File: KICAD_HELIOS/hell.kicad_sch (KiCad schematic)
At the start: 27 parts, among them J1 Conn_01x05, J3 NC3FAAH, J4 NC3MAAH, J5 ecran, SW1 SW_Push, SW2 SW_Push, U1 STM32F103C6Tx, U2 AMS1117-3.3, U3 MAX485E, U4 R-78B2.5-2.0

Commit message: Fix: correction erreurs schéma, maj empreintes et ajout notes
- Résolution de toutes les erreurs ERC du schéma.
- Mise à jour des empreintes (Importation d'empreintes non présentes dans KiCad, composants passifs...).
- Ajout de Warning_KiCad_fichier_temporaire.md : liste des questions et problèmes à régler.
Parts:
- C1, C10, C12, C2, C3, C4, C5, C6, C7, C8, C9: footprint (none) -> Capacitor_SMD:C_0805_2012Metric
- D1, D2: footprint (none) -> LED_SMD:LED_0805_2012Metric
- J1, J5: footprint (none) -> Connector_PinHeader_2.54mm:PinHeader_1x05_P2.54mm_Vertical
- R1, R2: footprint (none) -> Resistor_SMD:R_0805_2012Metric
- R3, R4: footprint (none) -> Resistor_SMD:R_1210_3225Metric
- SW1, SW2: footprint (none) -> Button_Switch_THT:SW_PUSH_6mm
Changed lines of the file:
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@@
 			)
 		)
-		(property "Footprint" ""
+		(property "Footprint" "Capacitor_SMD:C_0805_2012Metric"
 			(at 34.29 100.33 0)
 			(effects
@@
 			)
 		)
-		(property "Footprint" ""
+		(property "Footprint" "Capacitor_SMD:C_0805_2012Metric"
 			(at 220.98 36.83 0)
 			(effects
@@
 			)
 		)
-		(property "Footprint" ""
+		(property "Footprint" "Capacitor_SMD:C_0805_2012Metric"
 			(at 201.93 67.31 0)
 			(effects
@@
 			)
 		)
-		(property "Footprint" ""
+		(property "Footprint" "Capacitor_SMD:C_0805_2012Metric"
 			(at 80.01 88.9 0)
 			(effects
@@
 			)
 		)
-		(property "Footprint" ""
+		(property "Footprint" "Resistor_SMD:R_1210_3225Metric"
 			(at 187.96 130.81 0)
 			(effects
@@
 			)
 		)
-		(property "Footprint" ""
+		(property "Footprint" "Resistor_SMD:R_0805_2012Metric"
 			(at 29.21 100.33 0)
 			(effects
@@
 			)
 		)
-		(property "Footprint" ""
+		(property "Footprint" "Resistor_SMD:R_1210_3225Metric"
 			(at 187.96 120.65 0)
 			(effects
@@
 			)
 		)
-		(property "Footprint" ""
+		(property "Footprint" "Capacitor_SMD:C_0805_2012Metric"
 			(at 101.6 88.9 0)
 			(effects
@@
 			)
 		)
-		(property "Footprint" ""
+		(property "Footprint" "Capacitor_SMD:C_0805_2012Metric"
 			(at 86.36 88.9 0)
 			(effects
@@
 			)
 		)
-		(property "Footprint" ""
+		(property "Footprint" "Button_Switch_THT:SW_PUSH_6mm"
 			(at 149.86 127 0)
 			(effects
@@
 			)
 		)
-		(property "Footprint" ""
+		(property "Footprint" "LED_SMD:LED_0805_2012Metric"
 			(at 194.31 130.81 0)
 			(effects
@@
 			)
 		)
-		(property "Footprint" ""
+		(property "Footprint" "Connector_PinHeader_2.54mm:PinHeader_1x05_P2.54mm_Vertical"
 			(at 106.68 116.84 0)
 			(effects
@@
 			)
 		)
-		(property "Footprint" ""
+		(property "Footprint" "LED_SMD:LED_0805_2012Metric"
 			(at 194.31 120.65 0)
 			(effects
@@
 			)
 		)
-		(property "Footprint" ""
+		(property "Footprint" "Capacitor_SMD:C_0805_2012Metric"
 			(at 219.71 41.91 0)
 			(effects
@@
 			)
 		)
-		(property "Footprint" ""
+		(property "Footprint" "Resistor_SMD:R_0805_2012Metric"
 			(at 34.29 105.41 0)
 			(effects
@@
 			)
 		)
-		(property "Footprint" ""
+		(property "Footprint" "Connector_PinHeader_2.54mm:PinHeader_1x05_P2.54mm_Vertical"
 			(at 180.34 99.06 0)
 			(effects
@@
 			)
 		)
-		(property "Footprint" ""
+		(property "Footprint" "Capacitor_SMD:C_0805_2012Metric"
 			(at 166.37 95.25 0)
 			(effects
@@
 			)
 		)
-		(property "Footprint" ""
+		(property "Footprint" "Capacitor_SMD:C_0805_2012Metric"
 			(at 232.41 67.31 0)
 			(effects
@@
 			)
 		)
-		(property "Footprint" ""
+		(property "Footprint" "Capacitor_SMD:C_0805_2012Metric"
 			(at 92.71 88.9 0)
 			(effects
@@
 			)
 		)
-		(property "Footprint" ""
+		(property "Footprint" "Button_Switch_THT:SW_PUSH_6mm"
 			(at 151.13 118.11 0)
 			(effects
@@
 			)
 		)
-		(property "Footprint" ""
+		(property "Footprint" "Capacitor_SMD:C_0805_2012Metric"
 			(at 110.49 88.9 0)
 			(effects

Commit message: changement à faire schématic
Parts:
- removed U4: R-78B2.5-2.0, Converter_DCDC:Converter_DCDC_RECOM_R-78B-2.0_THT, symbol Converter_DCDC:R-78B2.5-2.0
- added J2: Conn_ST_STDC14, symbol Connector:Conn_ST_STDC14
- added U11: R-78B2.5-2.0, Converter_DCDC:Converter_DCDC_RECOM_R-78B-2.0_THT, symbol Converter_DCDC:R-78B2.5-2.0
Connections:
- net +24V: now also U11.1 (IN)
- net +5V: now also C7.1, U11.3 (OUT); no longer C7.2
- net GND: now also C7.2, U11.2 (GND); no longer C7.1
- new net: J2.5 (GND), J2.7 (GND)
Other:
- note added: "<-remplacer par ->"
- note added: "augmenter R"
- note added: "changer pour que ça soit mieux"
- note added: "changer valeur"
- note added: "condensateur"
- note added: "problème avec I2C"
- moved on the sheet: C6, C7, C8, C9, J1, U2

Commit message: correction (reste à calculer L)
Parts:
- removed J1: Conn_01x05, Connector_PinHeader_2.54mm:PinHeader_1x05_P2.54mm_Vertical, symbol Connector_Generic:Conn_01x05
- removed SW2: SW_Push, Button_Switch_THT:SW_PUSH_6mm, symbol Switch:SW_Push
- added C24: 100n, Capacitor_SMD:C_0805_2012Metric, symbol Device:C_Small
- added C25, C26: 10n, Capacitor_SMD:C_0805_2012Metric, symbol Device:C_Small
- added R13, R14, R15, R6: 10k, Resistor_SMD:R_1210_3225Metric, symbol Device:R_Small
- added R5: 1k, Resistor_SMD:R_1210_3225Metric, symbol Device:R_Small
- added SW3, SW4: SW_Push, Button_Switch_THT:SW_PUSH_6mm, symbol Switch:SW_Push
- C10: value 100u -> 1u
- C6, C7: value 100n -> 10u
- C9: value 10u -> 22u
- D1, D2: MPN (none) -> 150060RS55040
- R1: value 10k -> 1k; footprint Resistor_SMD:R_0805_2012Metric -> Resistor_SMD:R_1210_3225Metric
- R3, R4: value 330 -> 1k6
- U11: value R-78B2.5-2.0 -> R-78B5.0-2.0; MPN (none) -> R-78B5.0-2.0
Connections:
- net NRST is gone; now on net +3.3V: C12.2, U1.7 (NRST)
- net +3.3V: now also J2.12 (~{RST}), J2.3 (VCC), R1.2, R15.1, R5.2, R6.1, SW3.2; no longer R1.1, SW1.2
- net +5V: now also C24.1
- net BOUTTON_1: now also C25.1, R13.1; no longer SW1.1
- net BOUTTON_2: now also C26.1, R14.1
- net Ecr_SCL: now also R1.1
- net Ecr_SDA: now also R5.1
- net GND: now also C12.1, J2.11 (GNDDetect), J2.5 (GND), J2.7 (GND), SW1.2, C24.2, C25.2, C26.2, SW3.1, SW4.2
- net SWCLK: now also J2.6 (JCLK/SWCLK)
- net SWDIO: now also J2.4 (JTMS/SWDIO)
- new net: R13.2, R6.2, SW1.1
- new net: R14.2, R15.2, SW4.1
- no-connect marks 23 -> 28
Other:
- note added: "1.7V @ 1mA"
- note removed: "<-remplacer par ->"
- note removed: "augmenter R"
- note removed: "changer pour que ça soit mieux"
- note removed: "changer valeur"
- note removed: "condensateur"
- note removed: "problème avec I2C"
- moved on the sheet: C12, D1, D2, J2, R3, R4, SW1

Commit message: schématic finie
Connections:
- net +3.3V: no longer C12.2, J2.12 (~{RST}), SW3.2, U1.7 (NRST)
- new net NRST: C12.2, J2.12 (~{RST}), SW3.2, U1.7 (NRST)
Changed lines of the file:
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@@
 	)
 	(junction
-		(at 26.67 91.44)
-		(diameter 0)
-		(color 0 0 0 0)
-	)
-	(junction
 		(at 213.36 29.21)
 		(diameter 0)
@@
 	(wire
 		(pts
-			(xy 26.67 90.17) (xy 26.67 91.44)
-		)
-		(stroke
-			(width 0)
-			(type default)
-		)
-	)
-	(wire
-		(pts
 			(xy 187.96 38.1) (xy 199.39 38.1)
 		)
@@
 					(unit 1)
 				)
-			)
-		)
-	)
-	(symbol
-		(lib_id "power:+3.3V")
-		(at 26.67 90.17 0)
-		(unit 1)
-		(exclude_from_sim no)
-		(in_bom yes)
-		(on_board yes)
-		(dnp no)
-		(fields_autoplaced yes)
-		(property "Reference" "#PWR07"
-			(at 26.67 93.98 0)
-			(effects
-				(font
-					(size 1.27 1.27)
-				)
-				(hide yes)
-			)
-		)
-		(property "Value" "+3.3V"
-			(at 26.67 85.09 0)
-			(effects
-				(font
-					(size 1.27 1.27)
-				)
-			)
-		)
-		(property "Footprint" ""
-			(at 26.67 90.17 0)
-			(effects
-				(font
-					(size 1.27 1.27)
-				)
-				(hide yes)
-			)
-		)
-		(property "Datasheet" ""
-			(at 26.67 90.17 0)
-			(effects
-				(font
-					(size 1.27 1.27)
-				)
-				(hide yes)
-			)
-		)
-		(property "Description" "Power symbol creates a global label with name \"+3.3V\""
-			(at 26.67 90.17 0)
-			(effects
-				(font
-					(size 1.27 1.27)
-				)
-				(hide yes)
-			)
-		)
-		(pin "1"
-		)
-		(instances
-			(project "hell"
-				(path "/c000bab8-8bf2-446c-9c19-e9a7fa645af1"
-					(reference "#PWR07")
-					(unit 1)
-				)

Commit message: schematic + empreinte
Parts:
- J2: footprint (none) -> Connector_PinHeader_1.27mm:PinHeader_2x07_P1.27mm_Vertical_SMD
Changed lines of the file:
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@@
 			)
 		)
-		(property "Footprint" ""
+		(property "Footprint" "Connector_PinHeader_1.27mm:PinHeader_2x07_P1.27mm_Vertical_SMD"
 			(at 102.87 161.29 0)
 			(effects

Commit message: update pcb
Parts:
- added H101, H102, H103, H104, H105, H106: MountingHole_Pad, MountingHole:MountingHole_3.2mm_M3_DIN965_Pad, symbol Mechanical:MountingHole_Pad
- added J105: Conn_01x02, Connector_AMASS:AMASS_XT30U-M_1x02_P5.0mm_Vertical, symbol Connector_Generic:Conn_01x02
- renumbered C6 to C101, C7 to C102, C8 to C103, C9 to C104, C24 to C105, C5 to C106, C4 to C107, C1 to C108, C2 to C109, C3 to C110, C10 to C111, C12 to C112, C26 to C113, C25 to C114, D1 to D101, D2 to D102, J3 to J101, J4 to J102, J5 to J103, J2 to J104, R15 to R101, R1 to R102, R5 to R103, R6 to R104, R14 to R105, R13 to R106, R2 to R107, R3 to R108, R4 to R109, SW3 to SW101, SW4 to SW102, SW1 to SW103, U11 to U101, U2 to U102, U3 to U103, U1 to U104
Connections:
- net +24V: now also J105.2 (Pin_2)
- net GND: now also H101.1, H102.1, H103.1, H104.1, H105.1, H106.1, J105.1 (Pin_1)

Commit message: Kicad PCB et changement de quelques empreintes
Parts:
- C101: footprint Capacitor_SMD:C_0805_2012Metric -> Capacitor_SMD:C_1206_3216Metric
- C102, C103: footprint Capacitor_SMD:C_0805_2012Metric -> Capacitor_SMD:C_0603_1608Metric
- C105, C106, C107, C108, C109, C110, C111, C112, C113, C114: footprint Capacitor_SMD:C_0805_2012Metric -> Capacitor_SMD:C_0402_1005Metric
- R104, R105, R106: footprint Resistor_SMD:R_1210_3225Metric -> Resistor_SMD:R_0805_2012Metric
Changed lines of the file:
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@@
 			)
 		)
-		(property "Footprint" "Capacitor_SMD:C_0805_2012Metric"
+		(property "Footprint" "Capacitor_SMD:C_0402_1005Metric"
 			(at 30.48 100.33 0)
 			(effects
@@
 			)
 		)
-		(property "Footprint" "Capacitor_SMD:C_0805_2012Metric"
+		(property "Footprint" "Capacitor_SMD:C_1206_3216Metric"
 			(at 187.96 33.02 0)
 			(effects
@@
 			)
 		)
-		(property "Footprint" "Capacitor_SMD:C_0805_2012Metric"
+		(property "Footprint" "Capacitor_SMD:C_0603_1608Metric"
 			(at 228.6 52.07 0)
 			(effects
@@
 			)
 		)
-		(property "Footprint" "Capacitor_SMD:C_0805_2012Metric"
+		(property "Footprint" "Capacitor_SMD:C_0402_1005Metric"
 			(at 80.01 88.9 0)
 			(effects
@@
 			)
 		)
-		(property "Footprint" "Capacitor_SMD:C_0805_2012Metric"
+		(property "Footprint" "Capacitor_SMD:C_0402_1005Metric"
 			(at 210.82 107.95 0)
 			(effects
@@
 			)
 		)
-		(property "Footprint" "Resistor_SMD:R_1210_3225Metric"
+		(property "Footprint" "Resistor_SMD:R_0805_2012Metric"
 			(at 220.98 97.79 0)
 			(effects
@@
 			)
 		)
-		(property "Footprint" "Resistor_SMD:R_1210_3225Metric"
+		(property "Footprint" "Resistor_SMD:R_0805_2012Metric"
 			(at 255.27 100.33 0)
 			(effects
@@
 			)
 		)
-		(property "Footprint" "Capacitor_SMD:C_0805_2012Metric"
+		(property "Footprint" "Capacitor_SMD:C_0402_1005Metric"
 			(at 101.6 88.9 0)
 			(effects
@@
 			)
 		)
-		(property "Footprint" "Capacitor_SMD:C_0805_2012Metric"
+		(property "Footprint" "Capacitor_SMD:C_0402_1005Metric"
 			(at 250.19 106.68 0)
 			(effects
@@
 			)
 		)
-		(property "Footprint" "Capacitor_SMD:C_0805_2012Metric"
+		(property "Footprint" "Capacitor_SMD:C_0402_1005Metric"
 			(at 86.36 88.9 0)
 			(effects
@@
 			)
 		)
-		(property "Footprint" "Capacitor_SMD:C_0805_2012Metric"
+		(property "Footprint" "Capacitor_SMD:C_0603_1608Metric"
 			(at 213.36 33.02 0)
 			(effects
@@
 			)
 		)
-		(property "Footprint" "Capacitor_SMD:C_0805_2012Metric"
+		(property "Footprint" "Capacitor_SMD:C_0402_1005Metric"
 			(at 152.4 67.31 0)
 			(effects
@@
 			)
 		)
-		(property "Footprint" "Capacitor_SMD:C_0805_2012Metric"
+		(property "Footprint" "Capacitor_SMD:C_0402_1005Metric"
 			(at 166.37 95.25 0)
 			(effects
@@
 			)
 		)
-		(property "Footprint" "Capacitor_SMD:C_0805_2012Metric"
+		(property "Footprint" "Capacitor_SMD:C_0402_1005Metric"
 			(at 92.71 88.9 0)
 			(effects
@@
 			)
 		)
-		(property "Footprint" "Resistor_SMD:R_1210_3225Metric"
+		(property "Footprint" "Resistor_SMD:R_0805_2012Metric"
 			(at 215.9 101.6 0)
 			(effects
@@
 			)
 		)
-		(property "Footprint" "Capacitor_SMD:C_0805_2012Metric"
+		(property "Footprint" "Capacitor_SMD:C_0402_1005Metric"
 			(at 110.49 88.9 0)
 			(effects

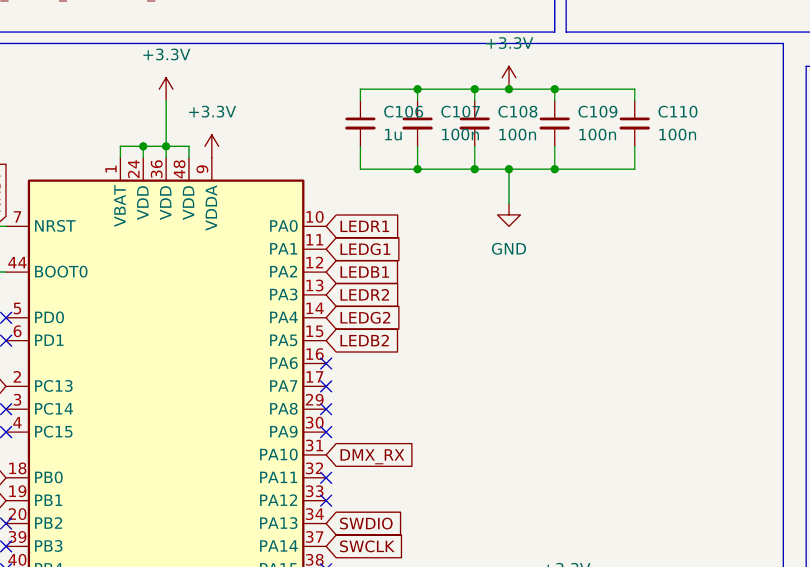
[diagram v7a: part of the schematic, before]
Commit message: Routage presque fini en attente de modification d'empreinte
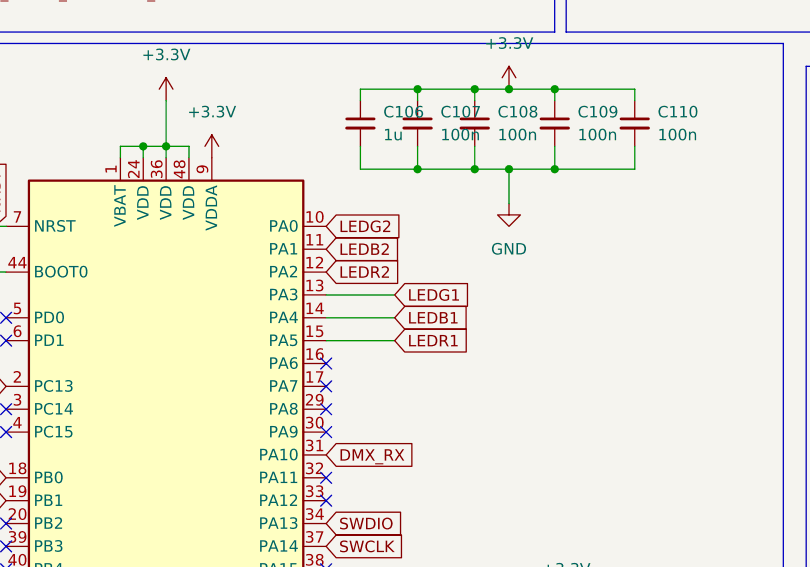
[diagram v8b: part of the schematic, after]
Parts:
- D101, D102: footprint LED_SMD:LED_0805_2012Metric -> LED_SMD:LED_0603_1608Metric
- R101, R102, R103, R108, R109: footprint Resistor_SMD:R_1210_3225Metric -> Resistor_SMD:R_0603_1608Metric
- R104, R105, R106, R107: footprint Resistor_SMD:R_0805_2012Metric -> Resistor_SMD:R_0603_1608Metric
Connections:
- net LEDB1: now also U104.14 (PA4); no longer U104.12 (PA2)
- net LEDB2: now also U104.11 (PA1); no longer U104.15 (PA5)
- net LEDG1: now also U104.13 (PA3); no longer U104.11 (PA1)
- net LEDG2: now also U104.10 (PA0); no longer U104.14 (PA4)
- net LEDR1: now also U104.15 (PA5); no longer U104.10 (PA0)
- net LEDR2: now also U104.12 (PA2); no longer U104.13 (PA3)
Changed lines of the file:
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@@
 	(wire
 		(pts
+			(xy 83.82 110.49) (xy 76.2 110.49)
+		)
+		(stroke
+			(width 0)
+			(type default)
+		)
+	)
+	(wire
+		(pts
 			(xy 220.98 100.33) (xy 220.98 101.6)
 		)
@@
 	(wire
 		(pts
+			(xy 83.82 107.95) (xy 76.2 107.95)
+		)
+		(stroke
+			(width 0)
+			(type default)
+		)
+	)
+	(wire
+		(pts
 			(xy 101.6 85.09) (xy 110.49 85.09)
 		)
@@
 	(wire
 		(pts
+			(xy 83.82 113.03) (xy 76.2 113.03)
+		)
+		(stroke
+			(width 0)
+			(type default)
+		)
+	)
+	(wire
+		(pts
 			(xy 119.38 148.59) (xy 115.57 148.59)
 		)
@@
 		)
 	)
+	(global_label "LEDR2"
+		(shape input)
+		(at 76.2 105.41 0)
+		(fields_autoplaced yes)
+		(effects
+			(font
+				(size 1.27 1.27)
+			)
+			(justify left)
+		)
+		(property "Intersheetrefs" "${INTERSHEET_REFS}"
+			(at 85.1118 105.41 0)
+			(effects
+				(font
+					(size 1.27 1.27)
+				)
+				(justify left)
+				(hide yes)
+			)
+		)
+	)
 	(global_label "LEDG1"
 		(shape input)
@@
 		)
 	)
-	(global_label "LED_1"
+	(global_label "LEDG2"
 		(shape input)
-		(at 40.64 128.27 180)
+		(at 76.2 100.33 0)
 		(fields_autoplaced yes)
 		(effects
@@
 				(size 1.27 1.27)
 			)
-			(justify right)
+			(justify left)
 		)
 		(property "Intersheetrefs" "${INTERSHEET_REFS}"
-			(at 32.0306 128.27 0)
+			(at 85.1118 100.33 0)
 			(effects
 				(font
 					(size 1.27 1.27)
 				)
-				(justify right)
+				(justify left)
 				(hide yes)
 			)
 		)
 	)
-	(global_label "DMX_N"
+	(global_label "LED_1"
 		(shape input)
-		(at 142.24 54.61 0)
+		(at 40.64 128.27 180)
 		(fields_autoplaced yes)
 		(effects
@@
 				(size 1.27 1.27)
 			)
-			(justify left)
+			(justify right)
 		)
 		(property "Intersheetrefs" "${INTERSHEET_REFS}"
-			(at 151.4542 54.61 0)
+			(at 32.0306 128.27 0)
 			(effects
 				(font
 					(size 1.27 1.27)
 				)
-				(justify left)
+				(justify right)
 				(hide yes)
 			)
 		)
 	)
-	(global_label "LEDG2"
+	(global_label "DMX_N"
 		(shape input)
-		(at 76.2 110.49 0)
+		(at 142.24 54.61 0)
 		(fields_autoplaced yes)
 		(effects
@@
 		)
 		(property "Intersheetrefs" "${INTERSHEET_REFS}"
-			(at 85.1118 110.49 0)
+			(at 151.4542 54.61 0)
 			(effects
 				(font
@@
 		)
 	)
-	(global_label "LEDR1"
+	(global_label "SWDIO"
 		(shape input)
-		(at 76.2 100.33 0)
+		(at 76.2 133.35 0)
 		(fields_autoplaced yes)
 		(effects
@@
 		)
 		(property "Intersheetrefs" "${INTERSHEET_REFS}"
-			(at 85.1118 100.33 0)
+			(at 85.0514 133.35 0)
 			(effects
 				(font
@@
 		)
 	)
-	(global_label "SWDIO"
+	(global_label "LEDG1"
 		(shape input)
-		(at 76.2 133.35 0)
+		(at 83.82 107.95 0)
 		(fields_autoplaced yes)
 		(effects
@@
 		)
 		(property "Intersheetrefs" "${INTERSHEET_REFS}"
-			(at 85.0514 133.35 0)
+			(at 92.7318 107.95 0)
 			(effects
 				(font
@@
 		)
 	)
-	(global_label "LEDR2"
-		(shape input)
-		(at 76.2 107.95 0)
-		(fields_autoplaced yes)
-		(effects
-			(font
-				(size 1.27 1.27)
-			)
-			(justify left)
-		)
-		(property "Intersheetrefs" "${INTERSHEET_REFS}"
-			(at 85.1118 107.95 0)
-			(effects
-				(font
-					(size 1.27 1.27)
-				)
-				(justify left)
-				(hide yes)
-			)
-		)
-	)
 	(global_label "LEDG2"
 		(shape input)
@@
 		)
 	)
-	(global_label "LEDB1"
-		(shape input)
-		(at 76.2 105.41 0)
-		(fields_autoplaced yes)
-		(effects
-			(font
-				(size 1.27 1.27)
-			)
-			(justify left)
-		)
-		(property "Intersheetrefs" "${INTERSHEET_REFS}"
-			(at 85.1118 105.41 0)
-			(effects
-				(font
-					(size 1.27 1.27)
-				)
-				(justify left)
-				(hide yes)
-			)
-		)
-	)
 	(global_label "BOUTTON_1"
 		(shape input)
@@
 		)
 	)
-	(global_label "LEDG1"
-		(shape input)
-		(at 76.2 102.87 0)
-		(fields_autoplaced yes)
-		(effects
-			(font
-				(size 1.27 1.27)
-			)
-			(justify left)
-		)
-		(property "Intersheetrefs" "${INTERSHEET_REFS}"
-			(at 85.1118 102.87 0)
-			(effects
-				(font
-					(size 1.27 1.27)
-				)
-				(justify left)
-				(hide yes)
-			)
-		)
-	)
 	(global_label "LEDR2"
 		(shape input)
@@
 		)
 	)
-	(global_label "LEDB2"
+	(global_label "LEDB1"
 		(shape input)
-		(at 76.2 113.03 0)
+		(at 83.82 110.49 0)
 		(fields_autoplaced yes)
 		(effects
@@
 		)
 		(property "Intersheetrefs" "${INTERSHEET_REFS}"
-			(at 85.1118 113.03 0)
+			(at 92.7318 110.49 0)
 			(effects
 				(font
@@
 		)
 	)
+	(global_label "LEDR1"
+		(shape input)
+		(at 83.82 113.03 0)
+		(fields_autoplaced yes)
+		(effects
+			(font
+				(size 1.27 1.27)
+			)
+			(justify left)
+		)
+		(property "Intersheetrefs" "${INTERSHEET_REFS}"
+			(at 92.7318 113.03 0)
+			(effects
+				(font
+					(size 1.27 1.27)
+				)
+				(justify left)
+				(hide yes)
+			)
+		)
+	)
 	(global_label "LED_1"
 		(shape input)
@@
 		)
 	)
+	(global_label "LEDB2"
+		(shape input)
+		(at 76.2 102.87 0)
+		(fields_autoplaced yes)
+		(effects
+			(font
+				(size 1.27 1.27)
+			)
+			(justify left)
+		)
+		(property "Intersheetrefs" "${INTERSHEET_REFS}"
+			(at 85.1118 102.87 0)
+			(effects
+				(font
+					(size 1.27 1.27)
+				)
+				(justify left)
+				(hide yes)
+			)
+		)
+	)
 	(global_label "DMX_P"
 		(shape input)
@@
 			)
 		)
-		(property "Footprint" "Resistor_SMD:R_1210_3225Metric"
+		(property "Footprint" "Resistor_SMD:R_0603_1608Metric"
 			(at 153.67 97.79 0)
 			(effects
@@
 			)
 		)
-		(property "Footprint" "Resistor_SMD:R_0805_2012Metric"
+		(property "Footprint" "Resistor_SMD:R_0603_1608Metric"
 			(at 220.98 97.79 0)
 			(effects
@@
 			)
 		)
-		(property "Footprint" "Resistor_SMD:R_1210_3225Metric"
+		(property "Footprint" "Resistor_SMD:R_0603_1608Metric"
 			(at 146.05 97.79 0)
 			(effects
@@
 			)
 		)
-		(property "Footprint" "Resistor_SMD:R_1210_3225Metric"
+		(property "Footprint" "Resistor_SMD:R_0603_1608Metric"
 			(at 151.13 129.54 0)
 			(effects
@@
 			)
 		)
-		(property "Footprint" "Resistor_SMD:R_0805_2012Metric"
+		(property "Footprint" "Resistor_SMD:R_0603_1608Metric"
 			(at 255.27 100.33 0)
 			(effects
@@
 			)
 		)
-		(property "Footprint" "Resistor_SMD:R_1210_3225Metric"
+		(property "Footprint" "Resistor_SMD:R_0603_1608Metric"
 			(at 151.13 119.38 0)
 			(effects
@@
 			)
 		)
-		(property "Footprint" "LED_SMD:LED_0805_2012Metric"
+		(property "Footprint" "LED_SMD:LED_0603_1608Metric"
 			(at 157.48 129.54 0)
 			(effects
@@
 			)
 		)
-		(property "Footprint" "LED_SMD:LED_0805_2012Metric"
+		(property "Footprint" "LED_SMD:LED_0603_1608Metric"
 			(at 157.48 119.38 0)
 			(effects
@@
 			)
 		)
-		(property "Footprint" "Resistor_SMD:R_0805_2012Metric"
+		(property "Footprint" "Resistor_SMD:R_0603_1608Metric"
 			(at 34.29 105.41 0)
 			(effects
@@
 			)
 		)
-		(property "Footprint" "Resistor_SMD:R_0805_2012Metric"
+		(property "Footprint" "Resistor_SMD:R_0603_1608Metric"
 			(at 215.9 101.6 0)
 			(effects
@@
 			)
 		)
-		(property "Footprint" "Resistor_SMD:R_1210_3225Metric"
+		(property "Footprint" "Resistor_SMD:R_0603_1608Metric"
 			(at 260.35 96.52 0)
 			(effects
